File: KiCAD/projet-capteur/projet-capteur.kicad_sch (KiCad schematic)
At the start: 5 parts, among them J1 Power, J2 Digital/PWM, J3 Analog, J4 Digital/PWM

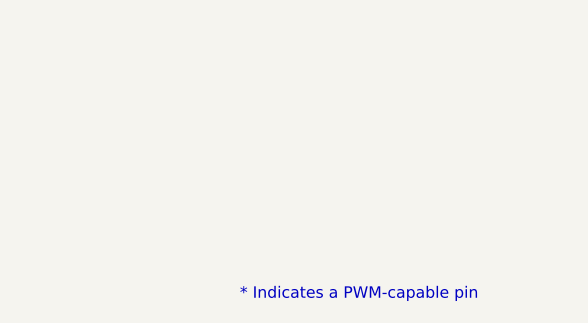
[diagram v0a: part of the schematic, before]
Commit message: Remis les empreintes perdues
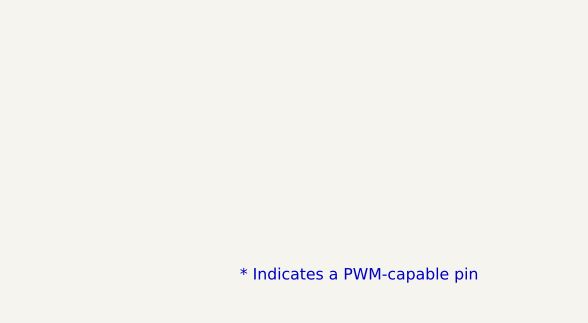
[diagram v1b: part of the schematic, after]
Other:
- company: (none) -> INSA Toulouse - 4A GP
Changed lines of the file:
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@@
 	(paper "A4")
 	(title_block
-		(date "mar. 31 mars 2015")
+		(date "2025-03-08")
+		(company "INSA Toulouse - 4A GP")
 	)
 	(junction
@@
 	(text "* Indicates a PWM-capable pin"
 		(exclude_from_sim no)
-		(at 177.8 180.34 0)
+		(at 177.8 178.308 0)
 		(effects
 			(font
@@
 	(label "RX{slash}0"
 		(at 74.93 77.47 180)
-		(fields_autoplaced yes)
 		(effects
 			(font
@@
 	(label "A2"
 		(at 21.59 64.77 0)
-		(fields_autoplaced yes)
 		(effects
 			(font
@@
 	(label "4"
 		(at 74.93 67.31 180)
-		(fields_autoplaced yes)
 		(effects
 			(font
@@
 	(label "2"
 		(at 74.93 72.39 180)
-		(fields_autoplaced yes)
 		(effects
 			(font
@@
 	(label "A3"
 		(at 21.59 67.31 0)
-		(fields_autoplaced yes)
 		(effects
 			(font
@@
 	(label "13"
 		(at 74.93 36.83 180)
-		(fields_autoplaced yes)
 		(effects
 			(font
@@
 	(label "12"
 		(at 74.93 39.37 180)
-		(fields_autoplaced yes)
 		(effects
 			(font
@@
 	(label "~{RESET}"
 		(at 19.05 36.83 0)
-		(fields_autoplaced yes)
 		(effects
 			(font
@@
 	(label "*10"
 		(at 74.93 44.45 180)
-		(fields_autoplaced yes)
 		(effects
 			(font
@@
 	(label "7"
 		(at 74.93 59.69 180)
-		(fields_autoplaced yes)
 		(effects
 			(font
@@
 	(label "SDA{slash}A4"
 		(at 74.93 29.21 180)
-		(fields_autoplaced yes)
 		(effects
 			(font
@@
 	(label "8"
 		(at 74.93 49.53 180)
-		(fields_autoplaced yes)
 		(effects
 			(font
@@
 	(label "*11"
 		(at 74.93 41.91 180)
-		(fields_autoplaced yes)
 		(effects
 			(font
@@
 	(label "*3"
 		(at 74.93 69.85 180)
-		(fields_autoplaced yes)
 		(effects
 			(font
@@
 	(label "A1"
 		(at 21.59 62.23 0)
-		(fields_autoplaced yes)
 		(effects
 			(font
@@
 	(label "TX{slash}1"
 		(at 74.93 74.93 180)
-		(fields_autoplaced yes)
 		(effects
 			(font
@@
 	(label "A0"
 		(at 21.59 59.69 0)
-		(fields_autoplaced yes)
 		(effects
 			(font
@@
 	(label "AREF"
 		(at 74.93 31.75 180)
-		(fields_autoplaced yes)
 		(effects
 			(font
@@
 	(label "Vin"
 		(at 26.67 26.67 270)
-		(fields_autoplaced yes)
 		(effects
 			(font
@@
 	(label "*6"
 		(at 74.93 62.23 180)
-		(fields_autoplaced yes)
 		(effects
 			(font
@@
 	(label "SCL{slash}A5"
 		(at 74.93 26.67 180)
-		(fields_autoplaced yes)
 		(effects
 			(font
@@
 	(label "*9"
 		(at 74.93 46.99 180)
-		(fields_autoplaced yes)
 		(effects
 			(font
@@
 	(label "*5"
 		(at 74.93 64.77 180)
-		(fields_autoplaced yes)
 		(effects
 			(font
@@
 	(label "IOREF"
 		(at 19.05 34.29 0)
-		(fields_autoplaced yes)
 		(effects
 			(font
@@
 	(label "SDA{slash}A4"
 		(at 21.59 69.85 0)
-		(fields_autoplaced yes)
 		(effects
 			(font
@@
 	(label "SCL{slash}A5"
 		(at 21.59 72.39 0)
-		(fields_autoplaced yes)
-		(effects
-			(font
+		(effects
+			(font

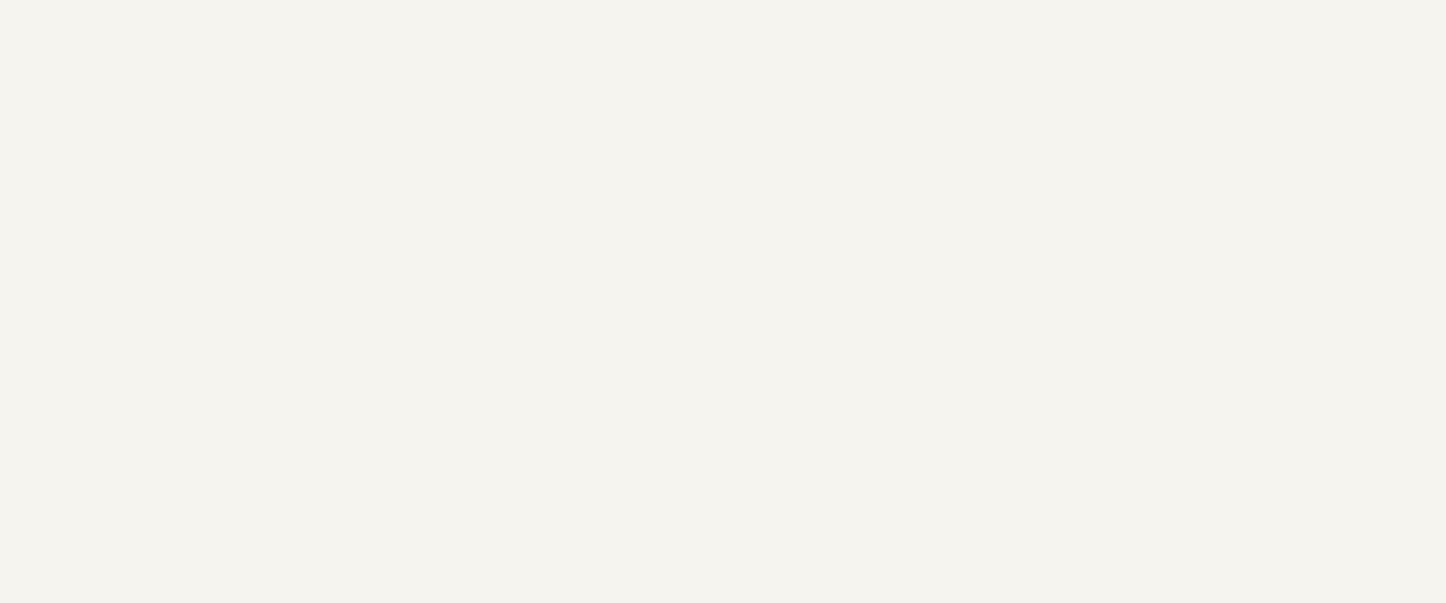
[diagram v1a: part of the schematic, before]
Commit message: Ajout ecran OLED + Schema
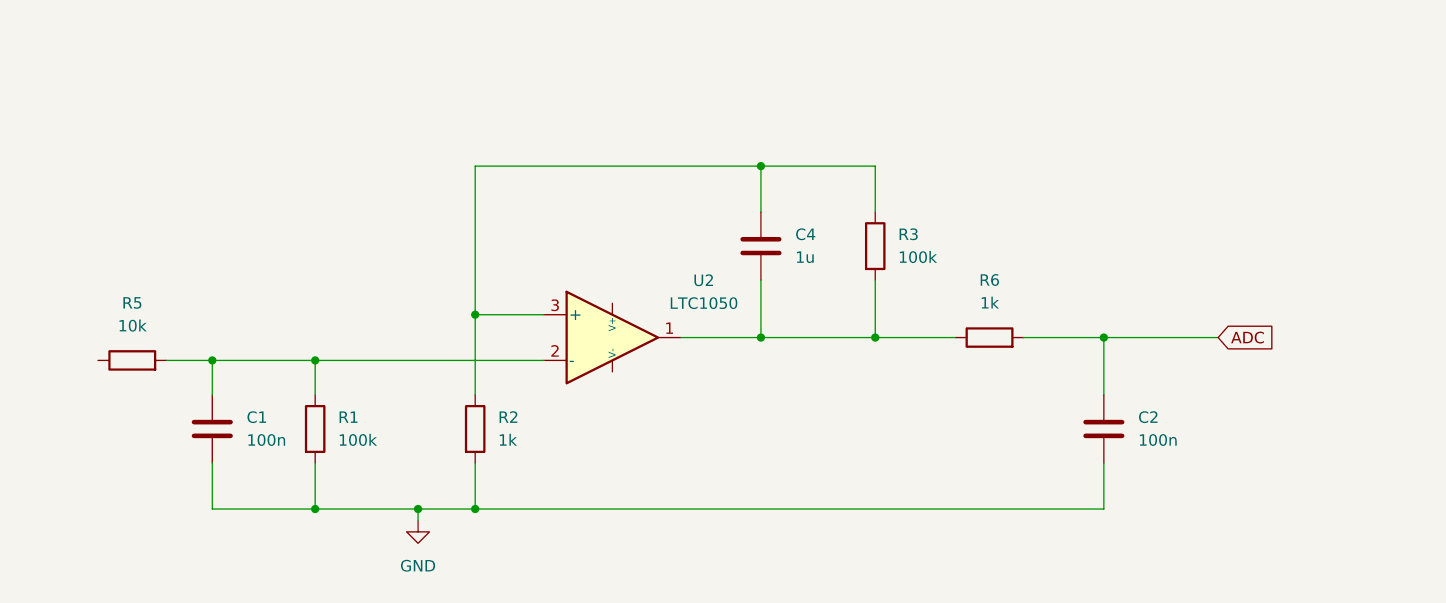
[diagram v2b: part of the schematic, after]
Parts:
- added C1, C2: 100n, symbol Device:C
- added C4: 1u, symbol Device:C
- added R1: 100k, Resistor_THT:R_Axial_DIN0207_L6.3mm_D2.5mm_P5.08mm_Vertical, symbol Device:R
- added R2, R6: 1k, symbol Device:R
- added R3: 100k, symbol Device:R
- added R5: 10k, symbol Device:R
- added U2: LTC1050, Package_DIP:DIP-8_W7.62mm, symbol MyLibGraphite:LTC1050
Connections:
- net GND: now also C1.2, C2.2, R1.2, R2.2
- new net: C4.2, R3.2, R6.1, U2.1
- new net: C1.1, R1.1, R5.2, U2.2 (-)
- new net: C4.1, R2.1, R3.1, U2.3 (+)
- new net ADC: C2.1, R6.2

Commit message: Ajout du HC-05
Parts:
- added U3: ~, MyLibEmpreinte:HC-05, symbol MyLibGraphite:HC-05_Bluetooth
- R1: renamed from R5; footprint (none) -> Resistor_THT:R_Axial_DIN0207_L6.3mm_D2.5mm_P5.08mm_Vertical
- R3: renamed from R2; footprint (none) -> Resistor_THT:R_Axial_DIN0207_L6.3mm_D2.5mm_P5.08mm_Vertical
- R4: renamed from R3; footprint (none) -> Resistor_THT:R_Axial_DIN0207_L6.3mm_D2.5mm_P5.08mm_Vertical
- R5: renamed from R6; footprint (none) -> Resistor_THT:R_Axial_DIN0207_L6.3mm_D2.5mm_P5.08mm_Vertical
- renumbered C4 to C2, C2 to C3, J3 to J2, J2 to J3, R1 to R2
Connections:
- net GND: now also U3.3 (GND)
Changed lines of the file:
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@@
+	(wire
+		(pts
+			(xy 175.26 78.74) (xy 175.26 81.28)
+		)
+		(stroke
+			(width 0)
+			(type default)
+		)
+	)
 	(wire
 		(pts
@@
 		(on_board yes)
 		(dnp no)
-		(property "Reference" "#PWR03"
+		(property "Reference" "#PWR105"
 			(at 31.75 30.48 0)
 			(effects
@@
 			(project "Arduino_Uno"
 				(path "/e63e39d7-6ac0-4ffd-8aa3-1841a4541b55"
-					(reference "#PWR03")
+					(reference "#PWR105")
 					(unit 1)
 				)
@@
 		(on_board yes)
 		(dnp no)
-		(property "Reference" "#PWR02"
+		(property "Reference" "#PWR104"
 			(at 29.21 30.48 0)
 			(effects
@@
 			(project "Arduino_Uno"
 				(path "/e63e39d7-6ac0-4ffd-8aa3-1841a4541b55"
-					(reference "#PWR02")
+					(reference "#PWR104")
 					(unit 1)
 				)
@@
 		(on_board yes)
 		(dnp no)
-		(property "Reference" "#PWR04"
+		(property "Reference" "#PWR106"
 			(at 31.75 58.42 0)
 			(effects
@@
 			(project "Arduino_Uno"
 				(path "/e63e39d7-6ac0-4ffd-8aa3-1841a4541b55"
-					(reference "#PWR04")
+					(reference "#PWR106")
 					(unit 1)
 				)
@@
 		(on_board yes)
 		(dnp no)
-		(property "Reference" "J2"
+		(property "Reference" "J3"
 			(at 57.15 24.13 0)
 			(effects
@@
 			(project "Arduino_Uno"
 				(path "/e63e39d7-6ac0-4ffd-8aa3-1841a4541b55"
-					(reference "J2")
+					(reference "J3")
 					(unit 1)
 				)
@@
 		(on_board yes)
 		(dnp no)
-		(property "Reference" "#PWR05"
+		(property "Reference" "#PWR102"
 			(at 64.77 58.42 0)
 			(effects
@@
 			(project "Arduino_Uno"
 				(path "/e63e39d7-6ac0-4ffd-8aa3-1841a4541b55"
-					(reference "#PWR05")
+					(reference "#PWR102")
 					(unit 1)
 				)
@@
 		(on_board yes)
 		(dnp no)
-		(property "Reference" "J3"
+		(property "Reference" "J2"
 			(at 39.37 57.15 0)
 			(effects
@@
 			(project "Arduino_Uno"
 				(path "/e63e39d7-6ac0-4ffd-8aa3-1841a4541b55"
-					(reference "J3")
+					(reference "J2")
 					(unit 1)
 				)
@@
 		(dnp no)
 		(fields_autoplaced yes)
-		(property "Reference" "R6"
+		(property "Reference" "R5"
 			(at 127 144.78 90)
 			(effects
@@
 			)
 		)
-		(property "Footprint" ""
+		(property "Footprint" "Resistor_THT:R_Axial_DIN0207_L6.3mm_D2.5mm_P5.08mm_Vertical"
 			(at 127 152.908 90)
 			(effects
@@
 			(project "projet-capteur"
 				(path "/e63e39d7-6ac0-4ffd-8aa3-1841a4541b55"
-					(reference "R6")
+					(reference "R5")
 					(unit 1)
 				)
@@
 		(dnp no)
 		(fields_autoplaced yes)
-		(property "Reference" "R1"
+		(property "Reference" "R2"
 			(at 54.61 160.0199 0)
 			(effects
@@
 			(project ""
 				(path "/e63e39d7-6ac0-4ffd-8aa3-1841a4541b55"
-					(reference "R1")
+					(reference "R2")
 					(unit 1)
 				)
@@
 		(on_board yes)
 		(dnp no)
-		(property "Reference" "#PWR01"
+		(property "Reference" "#PWR103"
 			(at 26.67 30.48 0)
 			(effects
@@
 			(project "Arduino_Uno"
 				(path "/e63e39d7-6ac0-4ffd-8aa3-1841a4541b55"
-					(reference "#PWR01")
+					(reference "#PWR103")
 					(unit 1)
 				)
@@
 		(dnp no)
 		(fields_autoplaced yes)
-		(property "Reference" "C4"
+		(property "Reference" "C2"
 			(at 105.41 139.6999 0)
 			(effects
@@
 			(project ""
 				(path "/e63e39d7-6ac0-4ffd-8aa3-1841a4541b55"
-					(reference "C4")
+					(reference "C2")
 					(unit 1)
 				)
@@
 		(dnp no)
 		(fields_autoplaced yes)
-		(property "Reference" "C2"
+		(property "Reference" "C3"
 			(at 143.51 160.0199 0)
 			(effects
@@
 			(project "projet-capteur"
 				(path "/e63e39d7-6ac0-4ffd-8aa3-1841a4541b55"
-					(reference "C2")
+					(reference "C3")
+					(unit 1)
+				)
+			)
+		)
+	)
+	(symbol
+		(lib_name "GND_2")
+		(lib_id "power:GND")
+		(at 175.26 81.28 0)
+		(unit 1)
+		(exclude_from_sim no)
+		(in_bom yes)
+		(on_board yes)
+		(dnp no)
+		(fields_autoplaced yes)
+		(property "Reference" "#PWR1"
+			(at 175.26 87.63 0)
+			(effects
+				(font
+					(size 1.27 1.27)
+				)
+				(hide yes)
+			)
+		)
+		(property "Value" "GND"
+			(at 175.26 86.36 0)
+			(effects
+				(font
+					(size 1.27 1.27)
+				)
+			)
+		)
+		(property "Footprint" ""
+			(at 175.26 81.28 0)
+			(effects
+				(font
+					(size 1.27 1.27)
+				)
+				(hide yes)
+			)
+		)
+		(property "Datasheet" ""
+			(at 175.26 81.28 0)
+			(effects
+				(font
+					(size 1.27 1.27)
+				)
+				(hide yes)
+			)
+		)
+		(property "Description" "Power symbol creates a global label with name \"GND\" , ground"
+			(at 175.26 81.28 0)
+			(effects
+				(font
+					(size 1.27 1.27)
+				)
+				(hide yes)
+			)
+		)
+		(pin "1"
+		)
+		(instances
+			(project ""
+				(path "/e63e39d7-6ac0-4ffd-8aa3-1841a4541b55"
+					(reference "#PWR1")
 					(unit 1)
 				)
@@
 		(dnp no)
 		(fields_autoplaced yes)
-		(property "Reference" "R5"
+		(property "Reference" "R1"
 			(at 31.75 147.32 90)
 			(effects
@@
 			)
 		)
-		(property "Footprint" ""
+		(property "Footprint" "Resistor_THT:R_Axial_DIN0207_L6.3mm_D2.5mm_P5.08mm_Vertical"
 			(at 31.75 155.448 90)
 			(effects
@@
 			(project "projet-capteur"
 				(path "/e63e39d7-6ac0-4ffd-8aa3-1841a4541b55"
-					(reference "R5")
+					(reference "R1")
 					(unit 1)
 				)
@@
 		(dnp no)
 		(fields_autoplaced yes)
-		(property "Reference" "#PWR6"
+		(property "Reference" "#PWR101"
 			(at 63.5 177.8 0)
 			(effects
@@
 			(project ""
 				(path "/e63e39d7-6ac0-4ffd-8aa3-1841a4541b55"
-					(reference "#PWR6")
+					(reference "#PWR101")
 					(unit 1)
 				)
@@
 		(dnp no)
 		(fields_autoplaced yes)
-		(property "Reference" "R2"
+		(property "Reference" "R3"
 			(at 72.39 160.0199 0)
 			(effects
@@
 			)
 		)
-		(property "Footprint" ""
+		(property "Footprint" "Resistor_THT:R_Axial_DIN0207_L6.3mm_D2.5mm_P5.08mm_Vertical"
 			(at 68.072 161.29 90)
 			(effects
@@
 			(project "projet-capteur"
 				(path "/e63e39d7-6ac0-4ffd-8aa3-1841a4541b55"
-					(reference "R2")
+					(reference "R3")
 					(unit 1)
 				)
@@
 		(dnp no)
 		(fields_autoplaced yes)
-		(property "Reference" "R3"
+		(property "Reference" "R4"
 			(at 116.84 139.6999 0)
 			(effects
@@
 			)
 		)
-		(property "Footprint" ""
+		(property "Footprint" "Resistor_THT:R_Axial_DIN0207_L6.3mm_D2.5mm_P5.08mm_Vertical"
 			(at 112.522 140.97 90)
 			(effects
@@
 			(project ""
 				(path "/e63e39d7-6ac0-4ffd-8aa3-1841a4541b55"
-					(reference "R3")
+					(reference "R4")
 					(unit 1)
 				)
@@
 					(unit 1)
 				)
+			)
+		)
+	)
+	(symbol
+		(lib_id "MyLibGraphite:HC-05_Bluetooth")
+		(at 177.8 72.39 0)
+		(unit 1)
+		(exclude_from_sim no)
+		(in_bom yes)
+		(on_board yes)
+		(dnp no)
+		(fields_autoplaced yes)
+		(property "Reference" "U3"
+			(at 191.77 69.2149 0)
+			(effects
+				(font
+					(size 1.27 1.27)
+				)
+				(justify left)
+			)
+		)
+		(property "Value" "~"
+			(at 191.77 71.12 0)
+			(effects
+				(font
+					(size 1.27 1.27)
+				)
+				(justify left)
+			)
+		)
+		(property "Footprint" "MyLibEmpreinte:HC-05"
+			(at 179.07 74.93 0)
+			(effects
+				(font
+					(size 1.27 1.27)
+				)
+				(hide yes)
+			)
+		)
+		(property "Datasheet" ""
+			(at 179.07 74.93 0)
+			(effects
+				(font
+					(size 1.27 1.27)
+				)
+				(hide yes)
+			)
+		)
+		(property "Description" ""
+			(at 179.07 74.93 0)
+			(effects
+				(font
+					(size 1.27 1.27)
+				)
+				(hide yes)
+			)
+		)
+		(pin "5"
+		)
+		(pin "2"
+		)
+		(pin "3"
+		)
+		(pin "6"
+		)
+		(pin "1"
+		)
+		(pin "4"
+		)
+		(instances
+			(project ""
+				(path "/e63e39d7-6ac0-4ffd-8aa3-1841a4541b55"
+					(reference "U3")
+					(unit 1)
+				)

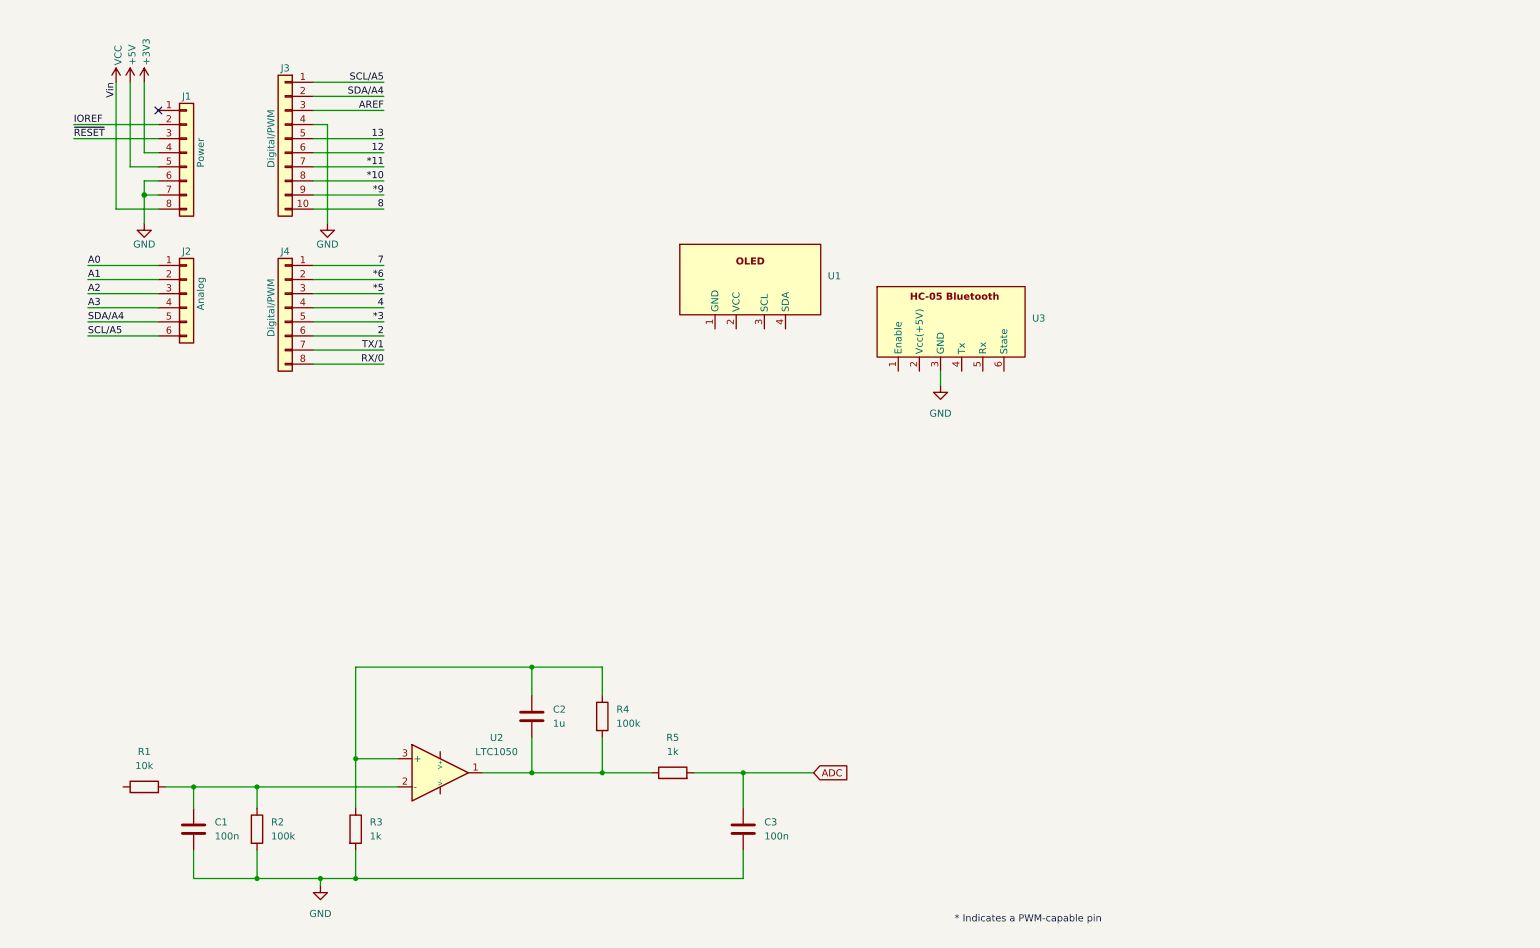
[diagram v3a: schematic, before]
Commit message: rajout des condesateur sur le pcb
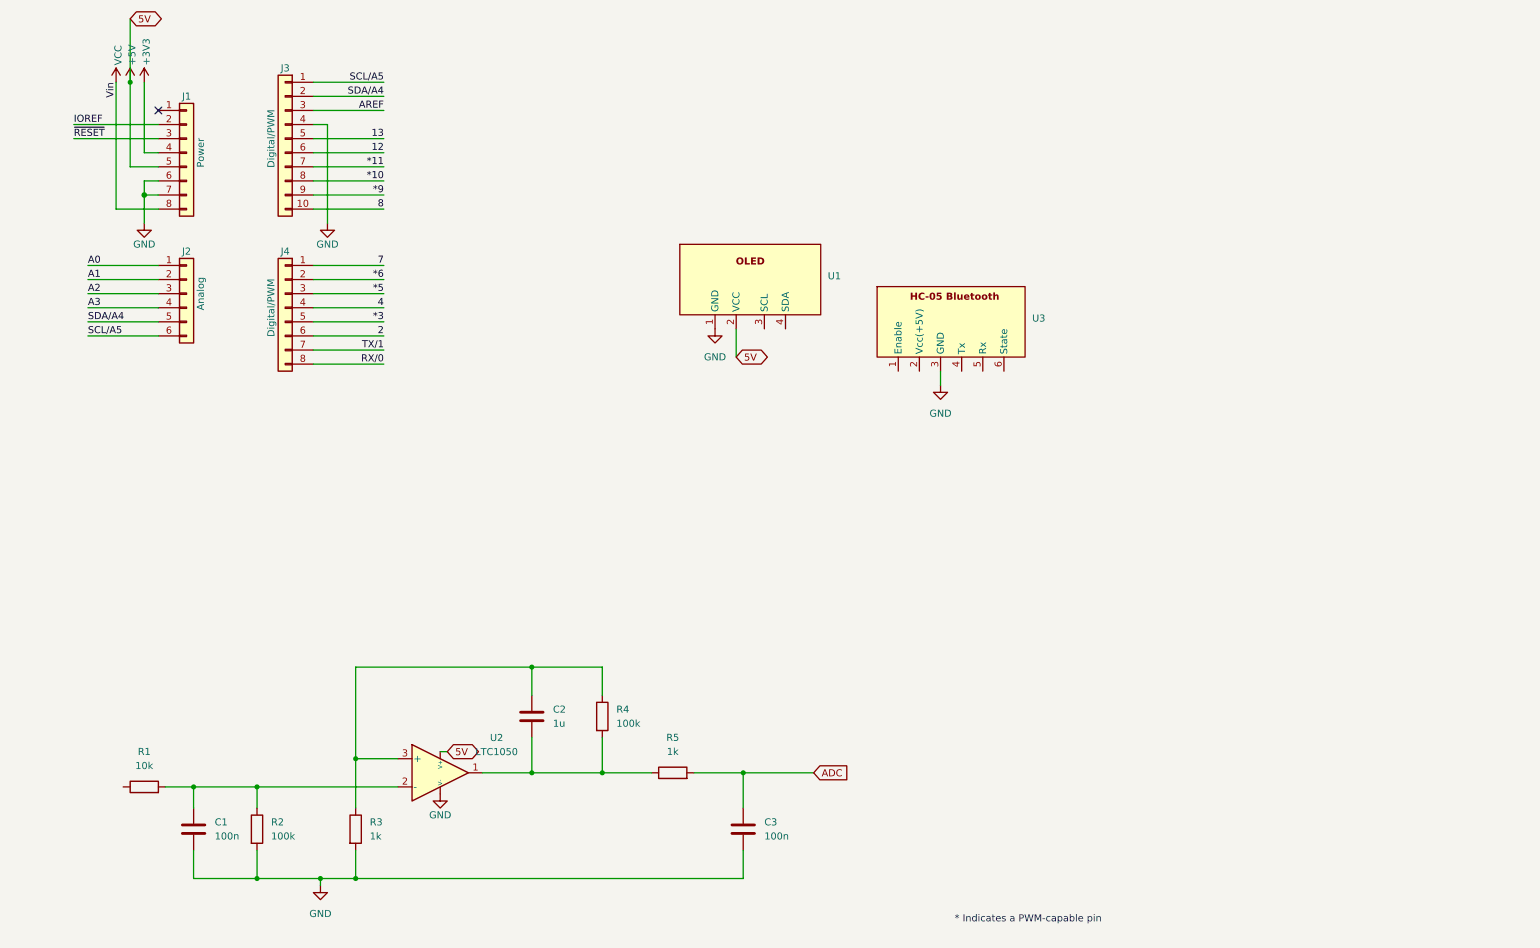
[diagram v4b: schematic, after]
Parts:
- C1, C2, C3: footprint (none) -> Resistor_THT:R_Axial_DIN0207_L6.3mm_D2.5mm_P5.08mm_Vertical
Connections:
- net +5V: now also U1.2 (VCC), U2. (V-)
- net GND: now also U1.1 (GND), U2. (V-)
